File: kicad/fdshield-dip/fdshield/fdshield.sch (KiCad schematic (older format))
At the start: 29 parts, among them J1 Conn_02x17_Odd_Even, P1 Power, P2 Analog, P3 Digital, P4 Digital, U1 74LS74, U3 74LS08, U4 74LS125, U5 23LCxxx, U6 74HCU04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

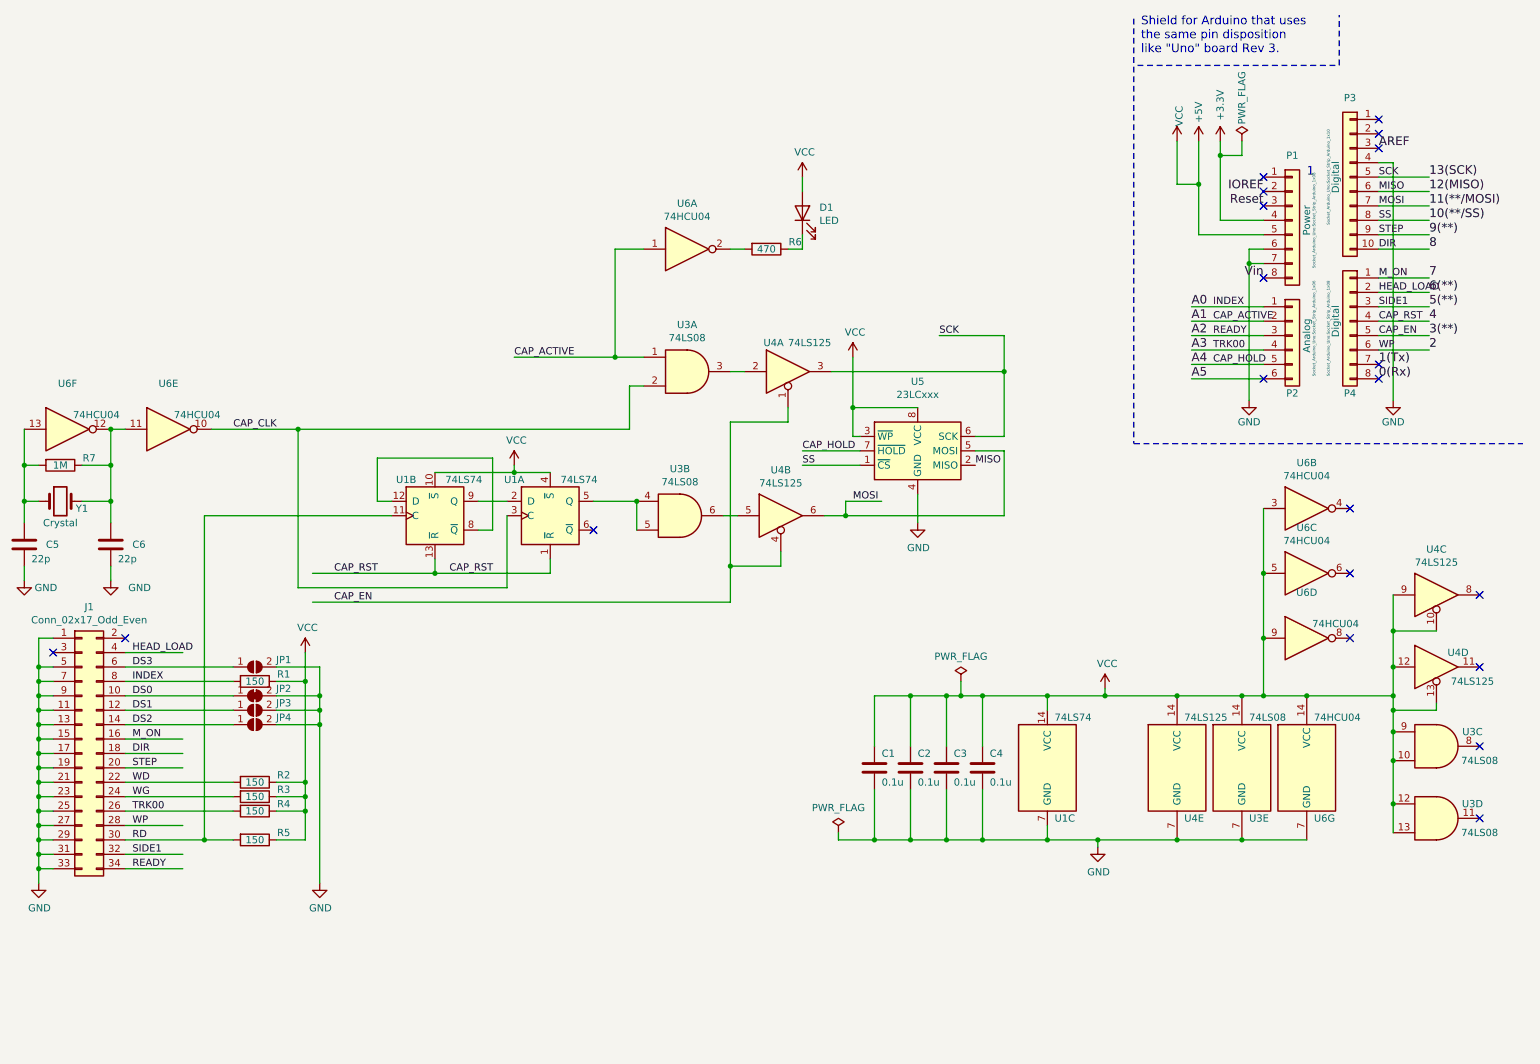
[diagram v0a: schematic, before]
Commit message: PCB FAB-F. Add write back feature
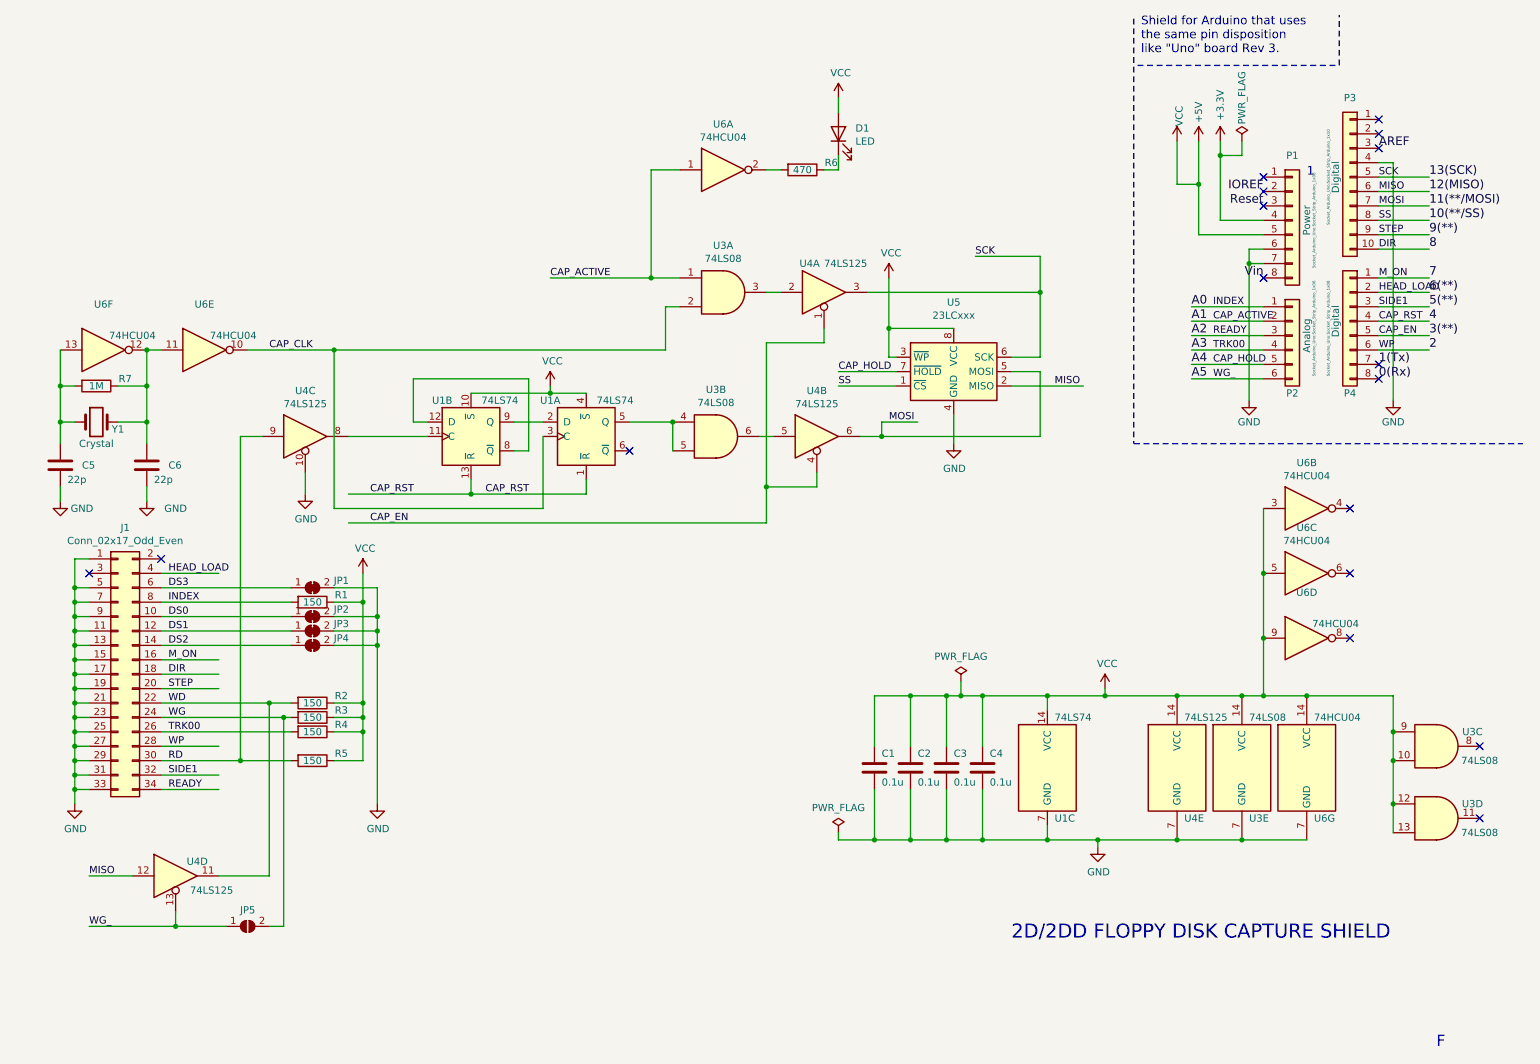
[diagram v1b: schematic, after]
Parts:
- removed JP1, JP3, JP4: SolderJumper_2_Open, Jumper:SolderJumper-2_P1.3mm_Open_Pad1.0x1.5mm, symbol Jumper:SolderJumper_2_Open
- added JP1, JP3, JP4: SolderJumper_2_Bridged, Jumper:SolderJumper-2_P1.3mm_Bridged_Pad1.0x1.5mm, symbol Jumper:SolderJumper_2_Bridged
- added JP5: SolderJumper_2_Open, Jumper:SolderJumper-2_P1.3mm_Open_Pad1.0x1.5mm, symbol Jumper:SolderJumper_2_Open
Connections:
- net labels added: WG_
- wire segments 221 -> 227
- no-connect marks 20 -> 17
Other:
- note added: "2D/2DD FLOPPY DISK CAPTURE SHIELD"
- note added: "F"
- moved on the sheet: C5, C6, D1, J1, JP2, R1, R2, R3, R4, R5, R6, R7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

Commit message: daily commit
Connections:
- wire segments 227 -> 234
- no-connect marks 17 -> 15
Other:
- note added: "G"
- note removed: "F"
- moved on the sheet: C5, C6, D1, R6, R7, U1A, U1B, U3A, U3B, U4A, U4B, U4C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

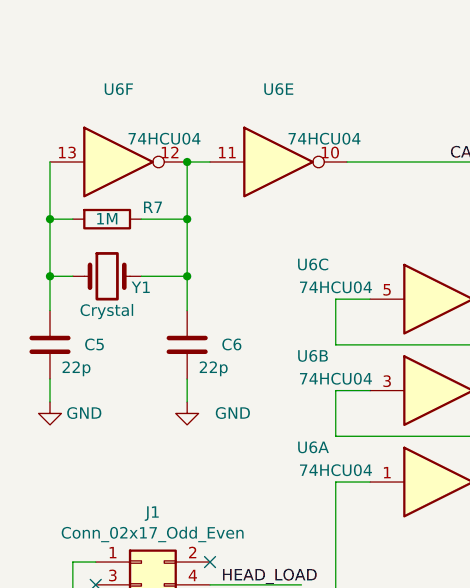
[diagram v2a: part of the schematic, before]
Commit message: Daily commit
- multiple address mark support (MB8877)
- fixed bug in drive type detection in fdcapture.ino
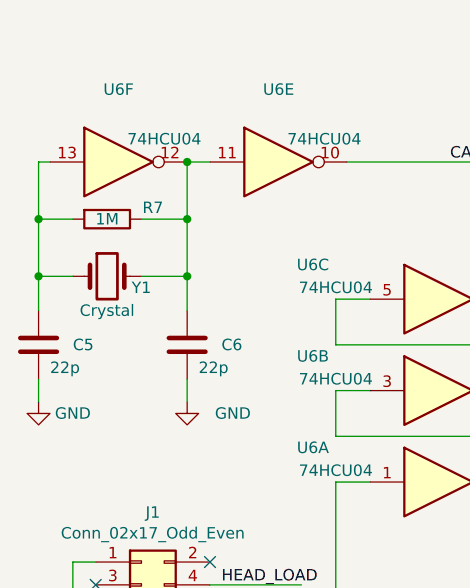
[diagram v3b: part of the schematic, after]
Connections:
- wire segments 234 -> 235
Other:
- moved on the sheet: C5
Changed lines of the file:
@@
 	1650 3550 1650 3450
 Wire Wire Line
-	1050 3450 1050 3550
+	1000 3450 1000 3550
 Wire Wire Line
 	1650 2500 1750 2500
@@
 	1450 3000 1650 3000
 Wire Wire Line
-	1150 3000 1050 3000
-Wire Wire Line
-	1050 3000 1050 2750
-Wire Wire Line
-	1050 2750 1050 2500
-Connection ~ 1050 2750
-Wire Wire Line
-	1050 2750 1150 2750
-Connection ~ 1050 3000
-Wire Wire Line
-	1050 3150 1050 3000
+	1150 3000 1000 3000
+Wire Wire Line
+	1000 3000 1000 2750
+Wire Wire Line
+	1000 2750 1000 2500
+Connection ~ 1000 2750
+Wire Wire Line
+	1000 2750 1150 2750
+Connection ~ 1000 3000
+Wire Wire Line
+	1000 3150 1000 3000
 $Comp
 L power:GND #PWR06
@@
 L power:GND #PWR05
 U 1 1 5F26E389
-P 1050 3550
-F 0 "#PWR05" H 1050 3300 50  0001 C CNN
-F 1 "GND" H 1200 3500 50  0000 C CNN
-F 2 "" H 1050 3550 50  0001 C CNN
-F 3 "" H 1050 3550 50  0001 C CNN
-	1    1050 3550
+P 1000 3550
+F 0 "#PWR05" H 1000 3300 50  0001 C CNN
+F 1 "GND" H 1150 3500 50  0000 C CNN
+F 2 "" H 1000 3550 50  0001 C CNN
+F 3 "" H 1000 3550 50  0001 C CNN
+	1    1000 3550
 	1    0    0    -1
 $EndComp
@@
 L Device:C C5
 U 1 1 5F26D99B
-P 1050 3300
-F 0 "C5" H 1200 3300 50  0000 L CNN
-F 1 "22p" H 1100 3200 50  0000 L CNN
-F 2 "Capacitor_THT:C_Disc_D3.0mm_W1.6mm_P2.50mm" H 1088 3150 50  0001 C CNN
-F 3 "~" H 1050 3300 50  0001 C CNN
-	1    1050 3300
+P 1000 3300
+F 0 "C5" H 1150 3300 50  0000 L CNN
+F 1 "22p" H 1050 3200 50  0000 L CNN
+F 2 "Capacitor_THT:C_Disc_D3.0mm_W1.6mm_P2.50mm" H 1038 3150 50  0001 C CNN
+F 3 "~" H 1000 3300 50  0001 C CNN
+	1    1000 3300
 	1    0    0    -1
 $EndComp
@@
 Wire Wire Line
 	3050 3100 3900 3100
+Wire Wire Line
+	1000 2500 1050 2500
 $EndSCHEMATC
